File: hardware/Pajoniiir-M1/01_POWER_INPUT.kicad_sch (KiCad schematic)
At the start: 19 parts, among them J1 5V_LOCKING_INPUT_TBD, U7 TPS259474ARPWR

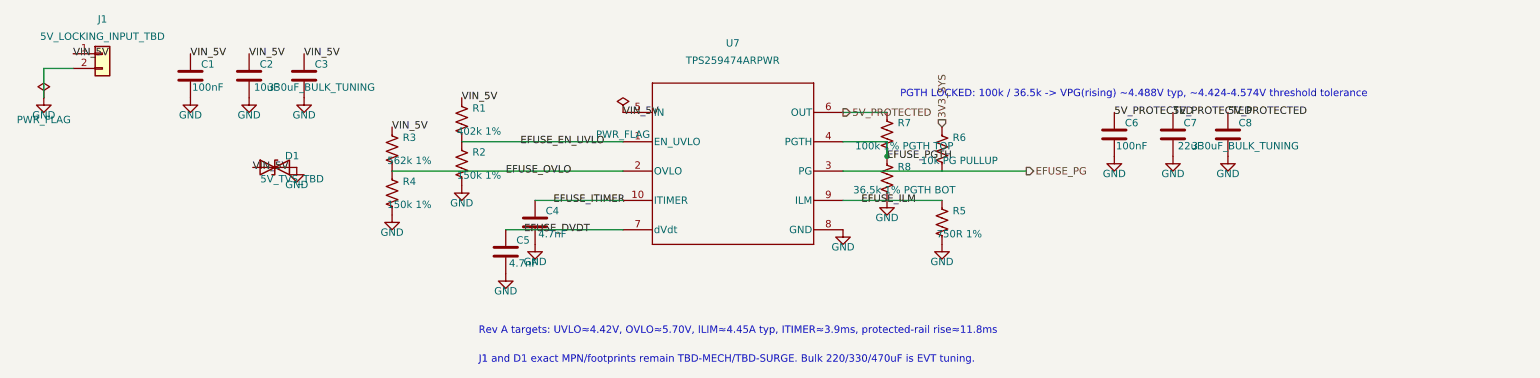
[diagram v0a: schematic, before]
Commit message: power: lock D1 input TVS source
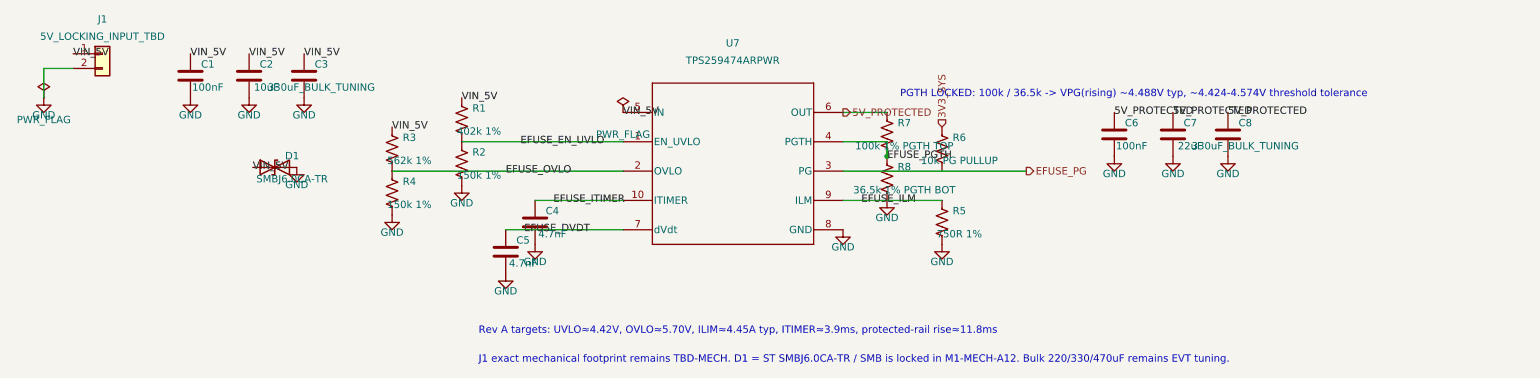
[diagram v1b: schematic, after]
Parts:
- D1: value 5V_TVS_TBD -> SMBJ6.0CA-TR; footprint (none) -> Diode_SMD:D_SMB
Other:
- note added: "J1 exact mechanical footprint remains TBD-MECH. D1 = ST SMBJ6.0CA-TR / SMB is locked in M1-MECH-A12. Bulk 220/330/470uF remains EVT tuning."
- note removed: "J1 and D1 exact MPN/footprints remain TBD-MECH/TBD-SURGE. Bulk 220/330/470uF is EVT tuning."
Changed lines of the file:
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@@
       (effects (font (size 1.27 1.27)))
     )
-    (property "Value" "5V_TVS_TBD" (at 62.69 61.69 0)
-      (effects (font (size 1.27 1.27)))
-    )
-    (property "Footprint" "" (at 59.69 59.69 0)
-      (effects (font (size 1.27 1.27)) (hide yes))
-    )
-    (property "Datasheet" "~" (at 59.69 59.69 0)
+    (property "Value" "SMBJ6.0CA-TR" (at 62.69 61.69 0)
+      (effects (font (size 1.27 1.27)))
+    )
+    (property "Footprint" "Diode_SMD:D_SMB" (at 59.69 59.69 0)
+      (effects (font (size 1.27 1.27)) (hide yes))
+    )
+    (property "Datasheet" "https://www.st.com/resource/en/datasheet/smbj.pdf" (at 59.69 59.69 0)
       (effects (font (size 1.27 1.27)) (hide yes))
     )
@@
     (effects (font (size 1.27 1.27)) (justify left))
   )
-  (text "J1 and D1 exact MPN/footprints remain TBD-MECH/TBD-SURGE. Bulk 220/330/470uF is EVT tuning."
+  (text "J1 exact mechanical footprint remains TBD-MECH. D1 = ST SMBJ6.0CA-TR / SMB is locked in M1-MECH-A12. Bulk 220/330/470uF remains EVT tuning."
     (exclude_from_sim no)
     (at 95 93 0)

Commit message: feat: establish board-first B8 pre-layout
Populate the live PCB with the complete schematic footprint/net set, preserve fail-closed mechanical gates, and isolate DSI506 as a qualified display profile. Add reproducible placement validation, ERC/BOM evidence, and synchronized project documentation.
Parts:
- added TP25: EFUSE_PG, TestPoint:TestPoint_Pad_D1.5mm, symbol Connector:TestPoint
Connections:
- net EFUSE_PG: now also TP25.1
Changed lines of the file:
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@@
   )
   (embedded_fonts no)
+  (symbol (lib_id "Connector:TestPoint") (at 225.425 85.725 0) (unit 1)
+    (exclude_from_sim no) (in_bom yes) (on_board yes) (dnp no)
+    (property "Reference" "TP25" (at 225.425 78.725 0) (effects (font (size 1.27 1.27))))
+    (property "Value" "EFUSE_PG" (at 225.425 80.725 0) (effects (font (size 1.27 1.27))))
+    (property "Footprint" "TestPoint:TestPoint_Pad_D1.5mm" (at 225.425 85.725 0) (effects (font (size 1.27 1.27)) (hide yes)))
+    (property "Datasheet" "~" (at 225.425 85.725 0) (effects (font (size 1.27 1.27)) (hide yes)))
+    (pin "1")
+    (instances (project "Pajoniiir-M1" (path "/2c8dd352-b7b8-4d9e-8f93-5dd43be2a100/31000001-6b2a-4a3a-8c91-000000000001" (reference "TP25") (unit 1))))
+  )
+  (label "EFUSE_PG" (at 225.425 85.725 0) (effects (font (size 1.27 1.27))))
 )
